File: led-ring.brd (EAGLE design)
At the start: 116.5 x 103 mm, 29 parts, among them IC8 MCP23017, X1 78127-1128, X2 78127-1128

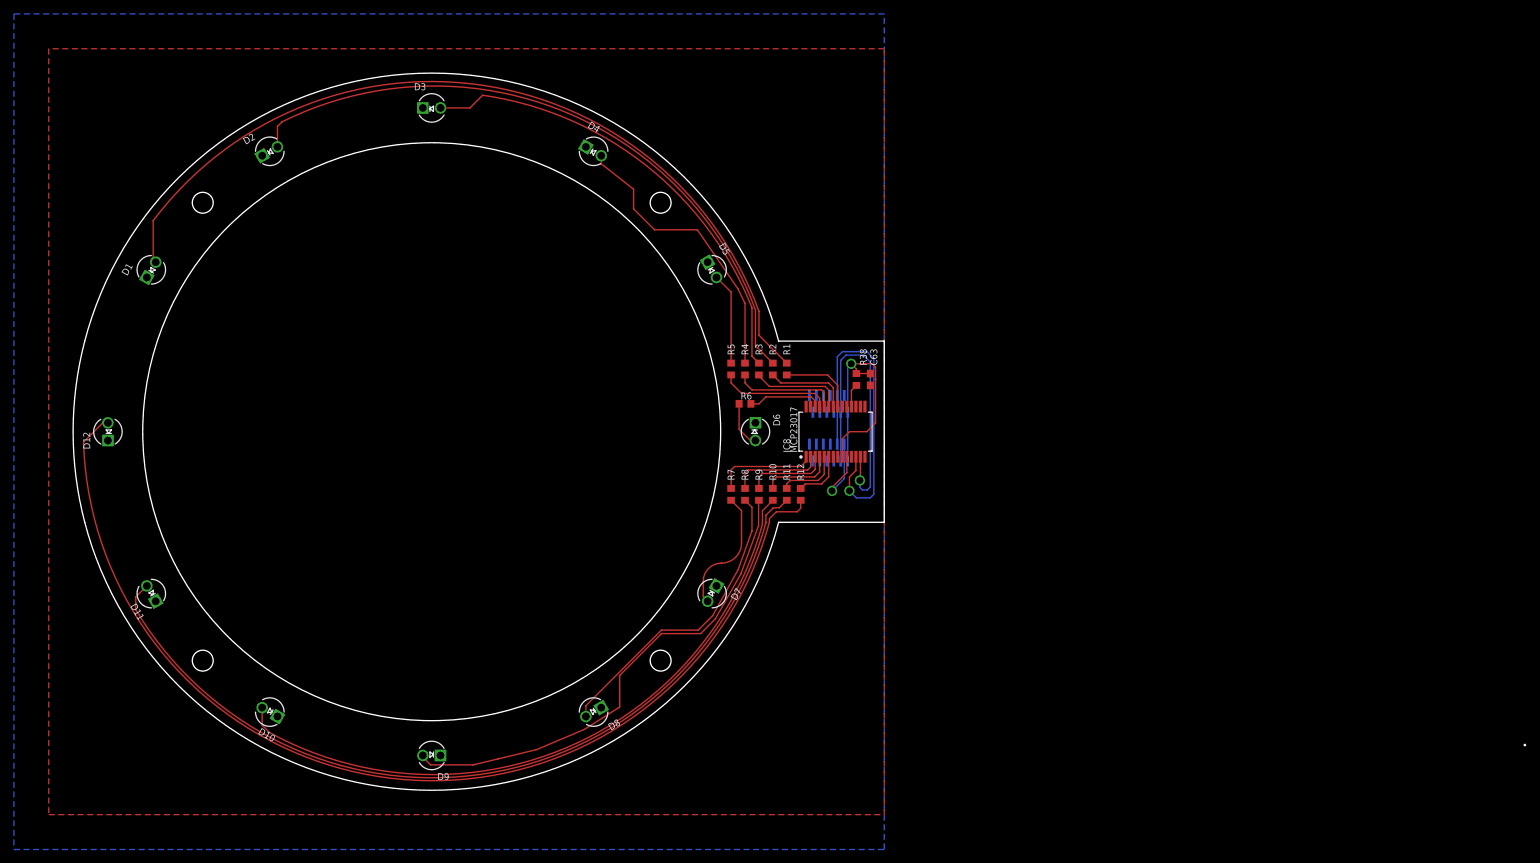
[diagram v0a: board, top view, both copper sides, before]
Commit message: beautified schematic | added i2c pull up resistors | beauty corrections on the board
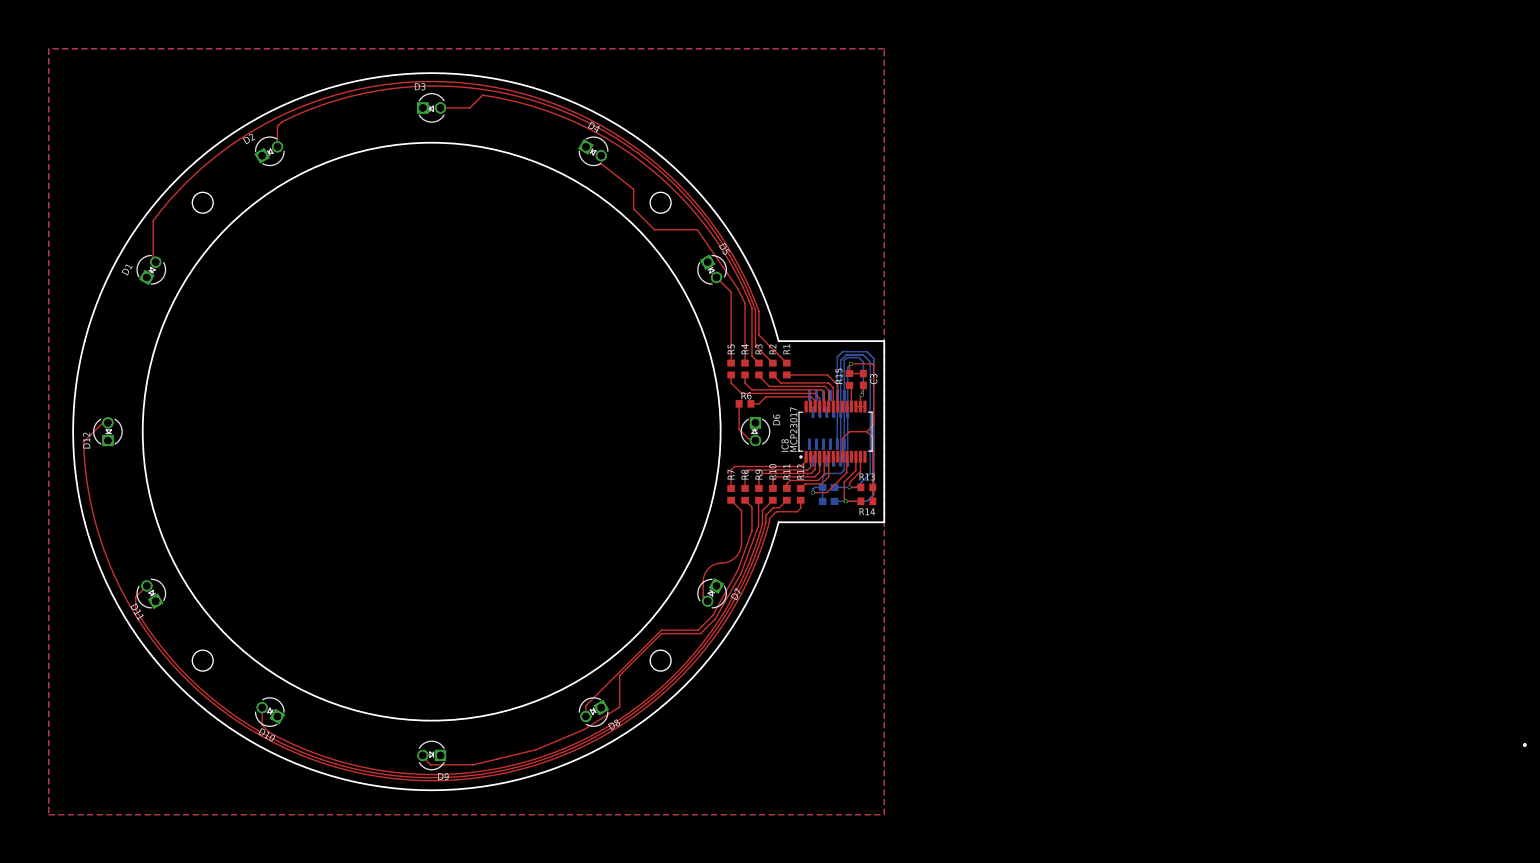
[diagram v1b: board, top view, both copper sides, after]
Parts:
- removed C63: 100n, rcl:C0603
- removed R38: 10k, rcl:R0603
- added C1, C2: 135p, rcl:C0603
- added C3: 100n, rcl:C0603
- added R13, R14: 1k, rcl:R0603
- added R15: 10k, rcl:R0603
- D1, D10, D11, D12, D2, D3, D4, D5, D6, D7, D8, D9: value LTL-1CHE -> WP710A10LSRD
- R1, R10, R11, R12, R2, R3, R4, R5, R6, R7, R8, R9: value (none) -> 1k
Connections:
- removed net I2C-INT: IC8.20
- net +3V3: now also C3.1, R13.1, R14.1, R15.2; no longer C63.1, R38.2
- net GND: now also C1.2, C2.2, C3.2; no longer C63.2
- net I2C-SCL: now also C1.1, R13.2
- net I2C-SDA: now also C2.1, R14.2
- net N$213: now also R15.1; no longer R38.1
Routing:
- net GND: track 13.4 -> 45.8 mm, vias 1 -> 2
- net +3V3: track 38.0 -> 47.8 mm
- net I2C-SCL: track 47.4 -> 53.4 mm
- net I2C-SDA: track 43.6 -> 48.1 mm
